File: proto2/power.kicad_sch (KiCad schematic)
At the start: 31 parts, among them Q15 2N7002, U15 NCP59300, U16 AQY282SX

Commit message: Working in suggestions from CFL review.
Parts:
- removed C50: 1uF, Capacitor_SMD:C_0805_2012Metric, symbol Device:C_Small
- removed C51: 47uF, Capacitor_SMD:C_0805_2012Metric, symbol Device:C_Small
- removed F16, F17, F18, F19: 500mA, Resistor_SMD:R_0805_2012Metric, symbol Device:Polyfuse_Small
- removed R21: 0R, Capacitor_SMD:C_1206_3216Metric, symbol Device:R_Small
- removed R54: 500R, Capacitor_SMD:C_0805_2012Metric, symbol Device:R_Small
- removed U15: NCP59300, Package_TO_SOT_SMD:TO-263-5_TabPin3, symbol BCR:NCP59300
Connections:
- no-connect marks 1 -> 0
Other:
- note removed: "DNP: C50 C51 R48 U13"
- moved on the sheet: Q15, R55, R56, R57, U16

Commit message: Changes suggested by CFL.
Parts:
- added R54, R58, R59, R60: 0R, Resistor_SMD:R_0805_2012Metric, symbol Device:R_Small
- C52, C53: Config (none) -> DNP
- PS1: value CUI_PDQE20_ISOLATED_DCDC -> CUI PDQE20-Q24-S5-D
- R19: value R Trim Up -> R Trim; Config (none) -> DNP
- R20: value R Trim Down -> R Trim; Config (none) -> DNP
- R53: LCSC (none) -> C17477
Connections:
- net Earth: now also R54.2
- net GND: now also R59.2
- net GNDPWR: now also R58.1, R60.1
- new net 24V_POUR: R54.1, R58.2
- new net 5V_POUR: R59.1, R60.2

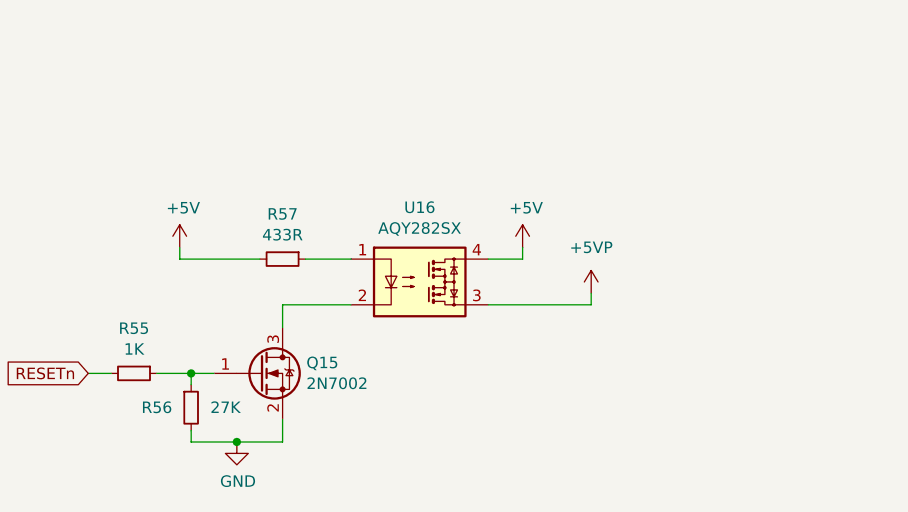
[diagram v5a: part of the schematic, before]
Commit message: Laying out new filters and some schematic updates.
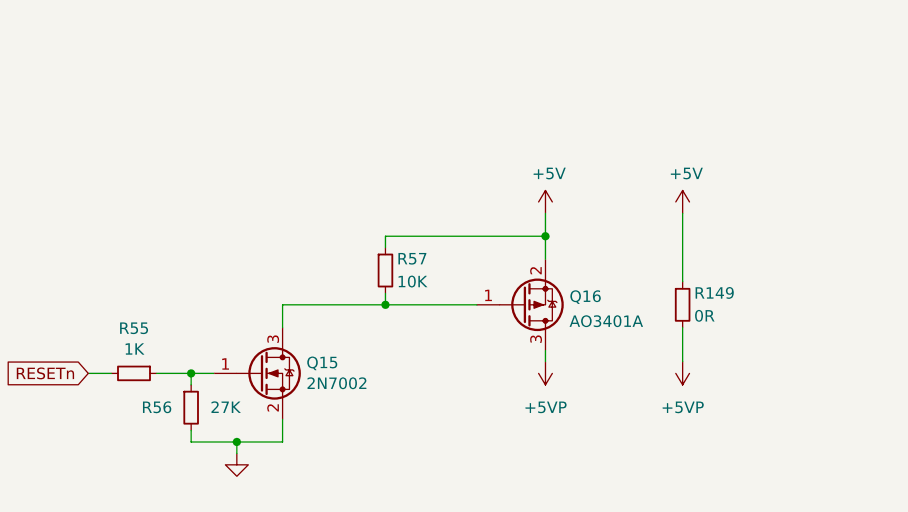
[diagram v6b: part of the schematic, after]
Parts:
- removed U16: AQY282SX, Package_SO:SO-4_4.4x4.3mm_P2.54mm, symbol Relay_SolidState:ASSR-1218
- added Q16: AO3401A, Package_TO_SOT_SMD:SOT-23, symbol Transistor_FET:AO3401A
- added R149: 0R, Resistor_SMD:R_0805_2012Metric, symbol Device:R_Small
- C44, C45: symbol Device:CP1_Small -> Device:C_Polarized_Small_US
- D15: symbol Device:D_Small_ALT -> Device:D_Small_Filled
- L43: symbol Device:L_Core_Ferrite_Small -> Device:L_Ferrite_Small
- PS1: symbol proto2-rescue:CUI_PDQE20_ISOLATED_DCDC-BCR -> BCR:CUI_PDQE20_ISOLATED_DCDC; Manufacturer (none) -> CUI; Part Number (none) -> PDQE20-Q24-S5-D
- Q15: LCSC (none) -> C8545
- R53, R54, R59: Config (none) -> DNP
- R57: value 433R -> 10K; LCSC C17694 -> C17414
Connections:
- net +5V: now also R57.1, Q16.2 (S), R149.1; no longer R57.2
- net +5VP: now also Q16.3 (D), R149.2
- net at Q15.3 (D): now also R57.2, Q16.1 (G)
- net Earth renamed GND-PWR
- net GND renamed GND-SIG
- net GNDPWR renamed GND-PE

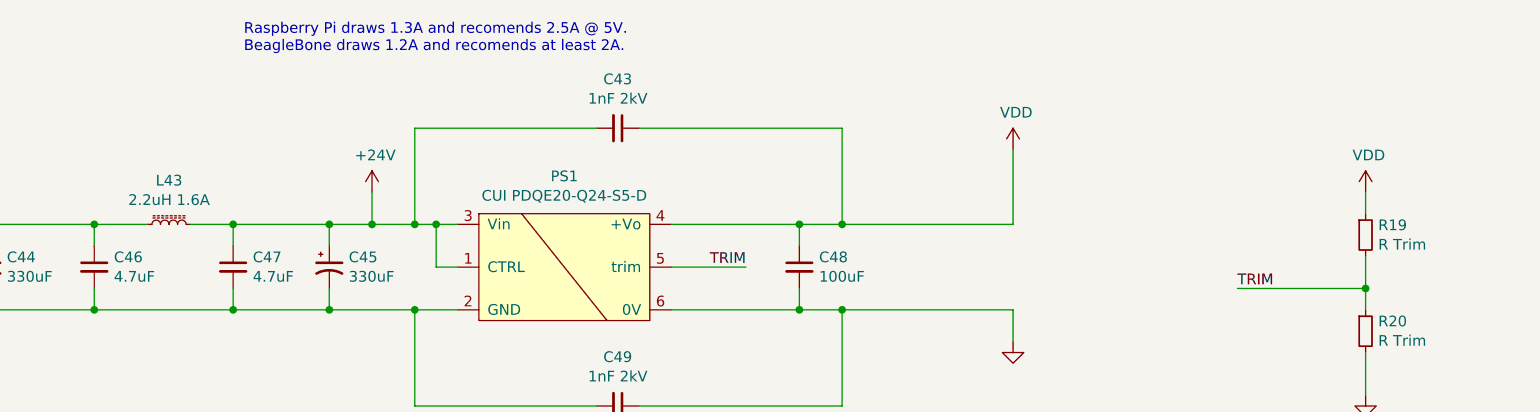
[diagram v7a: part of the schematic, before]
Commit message: Filter layout and some schematic fixes.
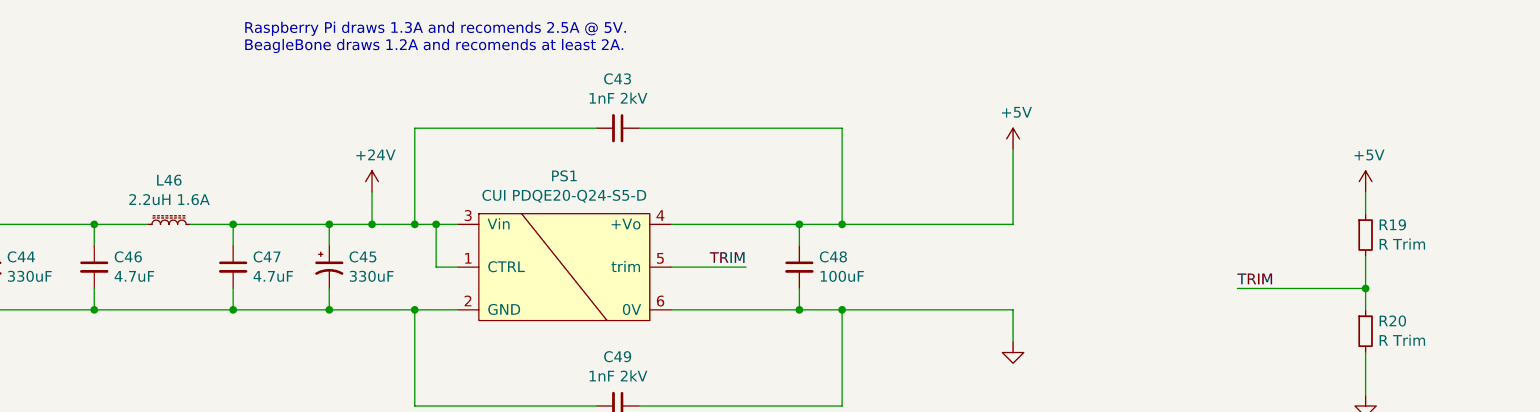
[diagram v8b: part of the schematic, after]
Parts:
- renumbered L43 to L46
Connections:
- net VDD is gone; now on net +5V: C43.1, C48.1, PS1.4 (+Vo), R19.1
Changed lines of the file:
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@@
   (symbol (lib_id "Device:L_Ferrite_Small") (at 68.58 44.45 90) (unit 1)
     (in_bom yes) (on_board yes)
-    (property "Reference" "L43" (id 0) (at 68.58 39.243 90))
+    (property "Reference" "L46" (id 0) (at 68.58 39.243 90))
     (property "Value" "2.2uH 1.6A" (id 1) (at 68.58 41.5544 90))
     (property "Footprint" "Inductor_BCR:Murata_LQH32PN2R2NN0L" (id 2) (at 68.58 44.45 0)
@@
     (pin "1")
     (pin "2")
-  )
-  (symbol (lib_id "power:VDD") (at 210.82 40.64 0) (unit 1)
-    (in_bom yes) (on_board yes)
-    (property "Reference" "#PWR0120" (id 0) (at 210.82 44.45 0)
-      (effects (font (size 1.27 1.27)) hide)
-    )
-    (property "Value" "VDD" (id 1) (at 211.201 36.2458 0))
-    (property "Footprint" "" (id 2) (at 210.82 40.64 0)
-      (effects (font (size 1.27 1.27)) hide)
-    )
-    (property "Datasheet" "" (id 3) (at 210.82 40.64 0)
-      (effects (font (size 1.27 1.27)) hide)
-    )
-    (pin "1")
   )
   (symbol (lib_id "BCR:CUI_PDQE20_ISOLATED_DCDC") (at 115.57 49.53 0) (unit 1)
@@
     (pin "2")
   )
-  (symbol (lib_id "power:VDD") (at 168.91 35.56 0) (unit 1)
-    (in_bom yes) (on_board yes)
-    (property "Reference" "#PWR0108" (id 0) (at 168.91 39.37 0)
-      (effects (font (size 1.27 1.27)) hide)
-    )
-    (property "Value" "VDD" (id 1) (at 169.291 31.1658 0))
-    (property "Footprint" "" (id 2) (at 168.91 35.56 0)
-      (effects (font (size 1.27 1.27)) hide)
-    )
-    (property "Datasheet" "" (id 3) (at 168.91 35.56 0)
-      (effects (font (size 1.27 1.27)) hide)
-    )
-    (pin "1")
-  )
   (symbol (lib_id "Device:R_Small") (at 135.89 123.19 0) (unit 1)
     (in_bom yes) (on_board yes)
@@
     (pin "1")
   )
+  (symbol (lib_id "power:+5V") (at 210.82 40.64 0) (unit 1)
+    (in_bom yes) (on_board yes)
+    (property "Reference" "#PWR?" (id 0) (at 210.82 44.45 0)
+      (effects (font (size 1.27 1.27)) hide)
+    )
+    (property "Value" "+5V" (id 1) (at 211.201 36.2458 0))
+    (property "Footprint" "" (id 2) (at 210.82 40.64 0)
+      (effects (font (size 1.27 1.27)) hide)
+    )
+    (property "Datasheet" "" (id 3) (at 210.82 40.64 0)
+      (effects (font (size 1.27 1.27)) hide)
+    )
+    (pin "1")
+  )
   (symbol (lib_id "Power_BCR:SIGGND") (at 210.82 64.77 0) (unit 1)
     (in_bom yes) (on_board yes) (fields_autoplaced)
@@
     (pin "2")
   )
+  (symbol (lib_id "power:+5V") (at 168.91 35.56 0) (unit 1)
+    (in_bom yes) (on_board yes)
+    (property "Reference" "#PWR?" (id 0) (at 168.91 39.37 0)
+      (effects (font (size 1.27 1.27)) hide)
+    )
+    (property "Value" "+5V" (id 1) (at 169.291 31.1658 0))
+    (property "Footprint" "" (id 2) (at 168.91 35.56 0)
+      (effects (font (size 1.27 1.27)) hide)
+    )
+    (property "Datasheet" "" (id 3) (at 168.91 35.56 0)
+      (effects (font (size 1.27 1.27)) hide)
+    )
+    (pin "1")
+  )
   (symbol (lib_id "Device:R_Small") (at 171.45 127 270) (unit 1)
